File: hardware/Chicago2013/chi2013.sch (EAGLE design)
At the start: 9 parts, among them IC1 TINY24/44/84-SSU, J1 AVR_SPI_PRG_6NS

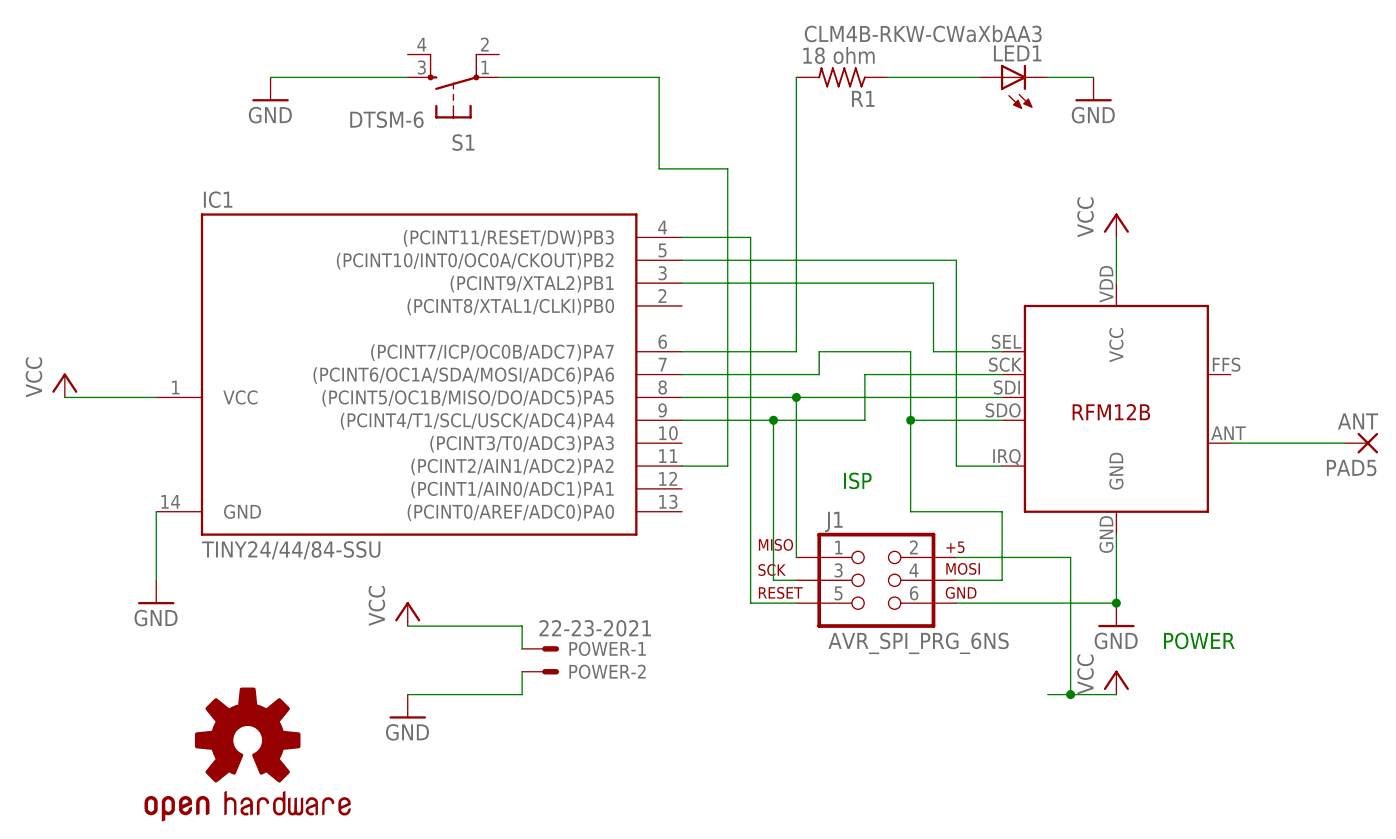
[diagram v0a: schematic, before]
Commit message: Removed old revisions and added two new ones. General repo cleanup.
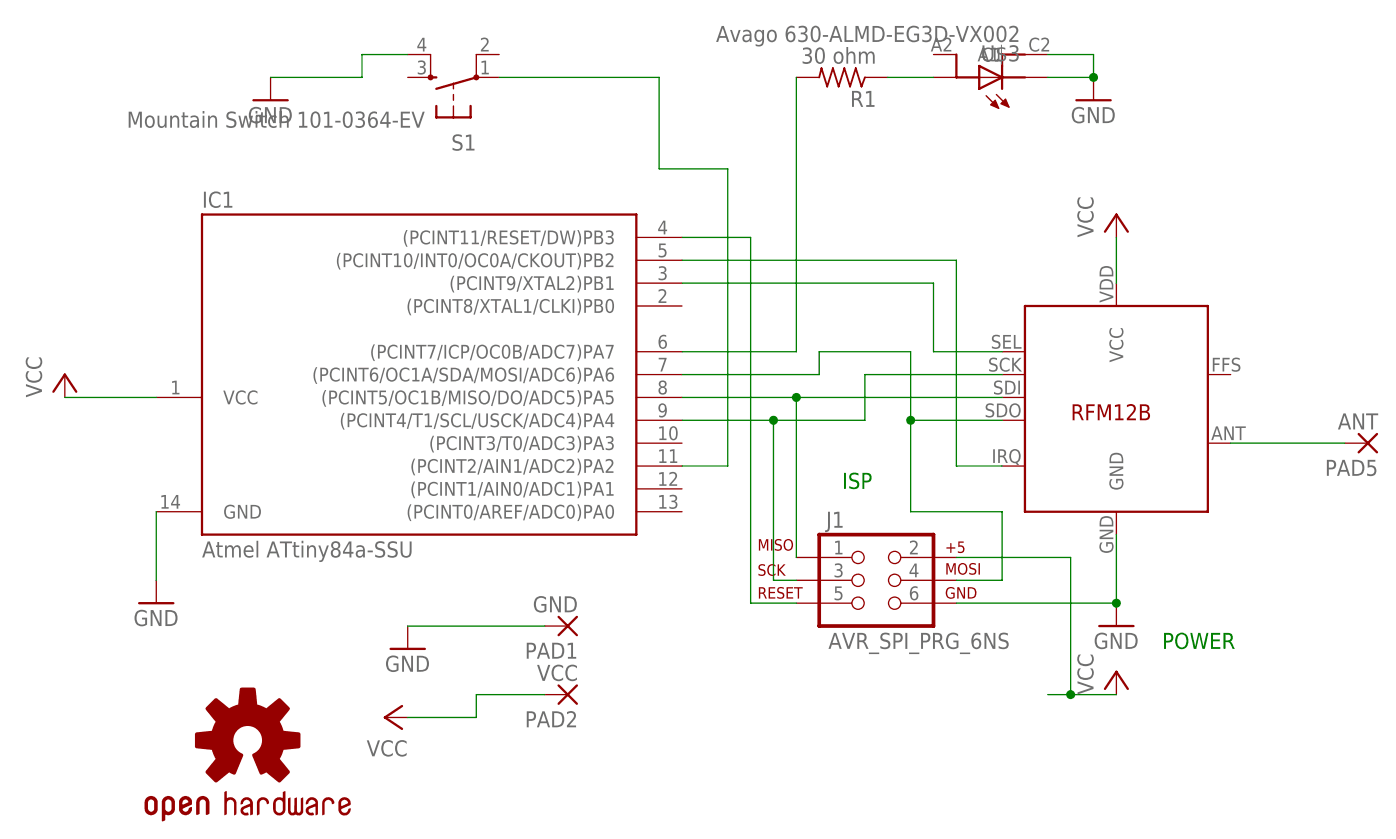
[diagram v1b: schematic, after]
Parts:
- removed LED1: CLM4B-RKW-CWaXbAA3, led:LEDP-LCC-4
- removed POWER: 22-23-2021, con-molex:22-23-2021
- added PAD1: GND, wirepad:2,15/1,0
- added PAD2: VCC, wirepad:2,15/1,0
- added U$3: Avago 630-ALMD-EG3D-VX002, ALMD-XX3D:ALMD-XX3D
- IC1: value TINY24/44/84-SSU -> Atmel ATtiny84a-SSU
- PAD5: device wirepad:WIREPAD2,54/1,0 -> wirepad:2,15/1,0
- R1: value 18 ohm -> 30 ohm
- RFM12B: value RFM12BN -> HopeRF RFM12B-433S1
- S1: value DTSM-6 -> Mountain Switch 101-0364-EV
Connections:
- net GND: now also PAD1.P, S1.4, U$3.C, U$3.C1; no longer LED1.C, POWER-2.S, S1.3
- net N$1: now also U$3.A; no longer LED1.A
- net VCC: now also PAD2.P; no longer POWER-1.S
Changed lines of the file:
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@@
 <?xml version="1.0" encoding="utf-8"?>
 <!DOCTYPE eagle SYSTEM "eagle.dtd">
-<eagle version="6.1">
+<eagle version="6.5.0">
 <drawing>
 <settings>
@@
 </classes>
 <parts>
-<part name="IC1" library="avr-7" deviceset="TINY24/44/84" device="-SSU"/>
-<part name="R1" library="resistor" deviceset="R-US_" device="R0805" value="18 ohm"/>
+<part name="IC1" library="avr-7" deviceset="TINY24/44/84" device="-SSU" value="Atmel ATtiny84a-SSU"/>
+<part name="R1" library="resistor" deviceset="R-US_" device="R0805" value="30 ohm"/>
 <part name="GND1" library="supply1" deviceset="GND" device=""/>
 <part name="P+2" library="supply1" deviceset="VCC" device=""/>
 <part name="GND3" library="supply1" deviceset="GND" device=""/>
 <part name="GND4" library="supply1" deviceset="GND" device=""/>
-<part name="PAD5" library="wirepad" deviceset="WIREPAD" device="2,54/1,0" value="ANT"/>
-<part name="LED1" library="led" deviceset="LED" device="P-LCC-4" value="CLM4B-RKW-CWaXbAA3"/>
+<part name="PAD5" library="wirepad" deviceset="2,15/1,0" device="" value="ANT"/>
 <part name="P+4" library="supply1" deviceset="VCC" device=""/>
 <part name="P+5" library="supply1" deviceset="VCC" device=""/>
 <part name="GND6" library="supply1" deviceset="GND" device=""/>
-<part name="S1" library="switch-tact" deviceset="DTSM-6" device=""/>
-<part name="RFM12B" library="JeeLabs" deviceset="RFM12B" device="N"/>
+<part name="S1" library="switch-tact" deviceset="DTSM-6" device="" value="Mountain Switch 101-0364-EV"/>
+<part name="RFM12B" library="JeeLabs" deviceset="RFM12B" device="N" value="HopeRF RFM12B-433S1"/>
 <part name="U$1" library="sfe-aesthetics" deviceset="OSHW-LOGO" device="S"/>
 <part name="J1" library="SparkFun-Connectors" deviceset="AVR_SPI_PRG_6" device="NS"/>
-<part name="POWER" library="con-molex" deviceset="22-23-2021" device=""/>
 <part name="GND2" library="supply1" deviceset="GND" device=""/>
 <part name="P+1" library="supply1" deviceset="VCC" device=""/>
+<part name="PAD1" library="wirepad" deviceset="2,15/1,0" device="" value="GND"/>
+<part name="PAD2" library="wirepad" deviceset="2,15/1,0" device="" value="VCC"/>
+<part name="U$3" library="ALMD-XX3D" deviceset="ALMD-XX3D" device="" value="Avago 630-ALMD-EG3D-VX002"/>
 </parts>
 <sheets>
@@
 <instance part="GND3" gate="1" x="53.34" y="83.82"/>
 <instance part="GND4" gate="1" x="55.88" y="25.4"/>
-<instance part="PAD5" gate="G$1" x="83.82" y="45.72" rot="R180"/>
-<instance part="LED1" gate="G$1" x="43.18" y="86.36" rot="R90"/>
+<instance part="PAD5" gate="1" x="83.82" y="45.72" rot="R180"/>
 <instance part="P+4" gate="VCC" x="-60.96" y="53.34"/>
 <instance part="P+5" gate="VCC" x="55.88" y="71.12"/>
@@
 <instance part="U$1" gate="G$1" x="-40.64" y="12.7"/>
 <instance part="J1" gate="G$1" x="27.94" y="30.48"/>
-<instance part="POWER" gate="-1" x="-7.62" y="22.86"/>
-<instance part="POWER" gate="-2" x="-7.62" y="20.32"/>
-<instance part="GND2" gate="1" x="-22.86" y="15.24"/>
-<instance part="P+1" gate="VCC" x="-22.86" y="27.94"/>
+<instance part="GND2" gate="1" x="-22.86" y="22.86"/>
+<instance part="P+1" gate="VCC" x="-25.4" y="15.24" rot="R90"/>
+<instance part="PAD1" gate="1" x="-5.08" y="25.4" rot="R180"/>
+<instance part="PAD2" gate="1" x="-5.08" y="17.78" rot="R180"/>
+<instance part="U$3" gate="G$1" x="43.18" y="86.36" rot="R90"/>
 </instances>
 <busses>
 </busses>
 <nets>
-<net name="GND" class="0">
+<net name="GND" class="1">
 <segment>
 <pinref part="IC1" gate="1" pin="GND"/>
@@
 </segment>
 <segment>
+<pinref part="U$3" gate="G$1" pin="C1"/>
 <pinref part="GND3" gate="1" pin="GND"/>
-<pinref part="LED1" gate="G$1" pin="C"/>
-<wire x1="53.34" y1="86.36" x2="48.26" y2="86.36" width="0.1524" layer="91"/>
+<wire x1="48.26" y1="88.9" x2="53.34" y2="88.9" width="0.1524" layer="91"/>
+<wire x1="53.34" y1="88.9" x2="53.34" y2="86.36" width="0.1524" layer="91"/>
+<pinref part="U$3" gate="G$1" pin="C"/>
+<wire x1="48.26" y1="86.36" x2="53.34" y2="86.36" width="0.1524" layer="91"/>
+<junction x="53.34" y="86.36"/>
+</segment>
+<segment>
+<pinref part="GND6" gate="1" pin="GND"/>
+<wire x1="-38.1" y1="86.36" x2="-27.94" y2="86.36" width="0.1524" layer="91"/>
+<wire x1="-27.94" y1="86.36" x2="-27.94" y2="88.9" width="0.1524" layer="91"/>
+<pinref part="S1" gate="G$1" pin="4"/>
+<wire x1="-27.94" y1="88.9" x2="-22.86" y2="88.9" width="0.1524" layer="91"/>
 </segment>
 <segment>
 <pinref part="GND2" gate="1" pin="GND"/>
-<pinref part="POWER" gate="-2" pin="S"/>
-<wire x1="-22.86" y1="17.78" x2="-10.16" y2="17.78" width="0.1524" layer="91"/>
-<wire x1="-10.16" y1="17.78" x2="-10.16" y2="20.32" width="0.1524" layer="91"/>
-</segment>
-<segment>
-<pinref part="GND6" gate="1" pin="GND"/>
-<pinref part="S1" gate="G$1" pin="3"/>
-<wire x1="-38.1" y1="86.36" x2="-22.86" y2="86.36" width="0.1524" layer="91"/>
-</segment>
-</net>
-<net name="VCC" class="0">
+<pinref part="PAD1" gate="1" pin="P"/>
+<wire x1="-22.86" y1="25.4" x2="-7.62" y2="25.4" width="0.1524" layer="91"/>
+</segment>
+</net>
+<net name="VCC" class="1">
 <segment>
 <pinref part="P+2" gate="VCC" pin="VCC"/>
@@
 <segment>
 <pinref part="P+1" gate="VCC" pin="VCC"/>
-<pinref part="POWER" gate="-1" pin="S"/>
-<wire x1="-22.86" y1="25.4" x2="-10.16" y2="25.4" width="0.1524" layer="91"/>
-<wire x1="-10.16" y1="25.4" x2="-10.16" y2="22.86" width="0.1524" layer="91"/>
+<wire x1="-22.86" y1="15.24" x2="-15.24" y2="15.24" width="0.1524" layer="91"/>
+<wire x1="-15.24" y1="15.24" x2="-15.24" y2="17.78" width="0.1524" layer="91"/>
+<pinref part="PAD2" gate="1" pin="P"/>
+<wire x1="-15.24" y1="17.78" x2="-7.62" y2="17.78" width="0.1524" layer="91"/>
 </segment>
 </net>
@@
 <segment>
 <pinref part="RFM12B" gate="G$1" pin="ANT"/>
-<pinref part="PAD5" gate="G$1" pin="P"/>
+<pinref part="PAD5" gate="1" pin="P"/>
 <wire x1="68.58" y1="45.72" x2="81.28" y2="45.72" width="0.1524" layer="91"/>
 </segment>
@@
 <net name="N$1" class="0">
 <segment>
-<pinref part="LED1" gate="G$1" pin="A"/>
 <pinref part="R1" gate="G$1" pin="1"/>
-<wire x1="40.64" y1="86.36" x2="30.48" y2="86.36" width="0.1524" layer="91"/>
-</segment>
-</net>
+<pinref part="U$3" gate="G$1" pin="A"/>
+<wire x1="30.48" y1="86.36" x2="35.56" y2="86.36" width="0.1524" layer="91"/>
+</segment>
+</net>
